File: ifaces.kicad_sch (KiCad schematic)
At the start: 33 parts, among them J3 MicroSD slot, J4 USB C, Q1 IRLML6401, Q2 BSS138, U3 USBLC6-2SC6

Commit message: more stuff
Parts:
- added J6: Display, symbol Connector:Conn_01x08_Pin
- added R16, R17, R18, R19, R20: 47k, Inductor_SMD:L_0805_2012Metric, symbol Device:R
- added R21: 1k, Inductor_SMD:L_0805_2012Metric, symbol Device:R
- added SW10, SW11, SW12, SW13, SW14, SW15, SW16, SW2, SW3, SW4, SW5, SW6, SW7, SW8, SW9: ~, symbol Switch:SW_Push_45deg
- added SW17: "OK", symbol Switch:SW_Push_45deg
- R10, R3, R4, R5, R6, R7, R8, R9: value 47R -> 27R
- R12: value 100k -> 47k
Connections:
- net +3V3: now also R21.2
- net GND: now also R16.1, R17.1, R18.1, R19.1, R20.1
- net DAT2: now reaches J3.1 (DAT2)
- net SD_DET: now reaches J3.10 (DET_A)
- net DAT3: now reaches J3.2 (DAT3/CD)
- net CMD: now reaches J3.3 (CMD)
- net CLK: now reaches J3.5 (CLK)
- net DAT0: now reaches J3.7 (DAT0)
- net DAT1: now reaches J3.8 (DAT1)
- new net: R21.1, SW17.2
- new net BOOT0: SW17.1
- new net COL_1: SW11.1, SW14.1, SW2.1, SW5.1, SW8.1
- new net COL_2: SW12.1, SW15.1, SW3.1, SW6.1, SW9.1
- new net COL_3: SW10.1, SW13.1, SW16.1, SW4.1, SW7.1
- new net ROW_1: R16.2, SW2.2, SW3.2, SW4.2
- new net ROW_2: R17.2, SW5.2, SW6.2, SW7.2
- new net ROW_3: R18.2, SW10.2, SW8.2, SW9.2
- new net ROW_4: R19.2, SW11.2, SW12.2, SW13.2
- new net ROW_5: R20.2, SW14.2, SW15.2, SW16.2
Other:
- note added: "Keyboard"
- moved on the sheet: C1, C2, C3, C4, C5, C6, D1, D2, D3, D4, D5, D6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

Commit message: imported SA868 - thanks, edgetriggered
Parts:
- renumbered C1 to C14, C2 to C15, C3 to C16, C6 to C17, C5 to C18, C4 to C19, D7 to D10, D8 to D11, D1 to D4, D2 to D5, D3 to D6, D4 to D7, D5 to D8, D6 to D9, FB1 to FB3, J3 to J4, J6 to J5, J4 to J6, Q2 to Q3, Q1 to Q4, R3 to R10, R4 to R11, R5 to R12, R6 to R13, R7 to R14, R8 to R15, R9 to R16, R10 to R17, R21 to R18, R16 to R19, R17 to R20, R18 to R21, R19 to R22, R20 to R23, R2 to R24, R1 to R25, R11 to R7, R13 to R8, R12 to R9, SW9 to SW10, SW12 to SW11, SW15 to SW12, SW4 to SW13, SW7 to SW14, SW10 to SW15, SW13 to SW16, SW16 to SW17, SW17 to SW2, SW2 to SW3, SW5 to SW4, SW8 to SW5, SW11 to SW6, SW14 to SW7, SW3 to SW8, SW6 to SW9, U3 to U5

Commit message: interfaces update
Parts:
- added C20: 10uF/10V, Capacitor_Tantalum_SMD:CP_EIA-3528-21_Kemet-B, symbol Device:C_Polarized
- added C21: 47uF/10V, Capacitor_Tantalum_SMD:CP_EIA-3528-21_Kemet-B, symbol Device:C_Polarized
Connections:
- net +3V3: now also J5.8 (Pin_8), Q4.2 (S), R9.2, C21.1
- net GND: now also J5.3 (Pin_3), C20.2, C21.2
- net ~{DISP_RST}: now reaches J5.1 (Pin_1)
- net at J5.2 (Pin_2): now also C20.1
- net ~{DISP_CE}: now reaches J5.4 (Pin_4)
- net DISP_D/C: now reaches J5.5 (Pin_5)
- net DISP_SDIN: now reaches J5.6 (Pin_6)
- net DISP_SCK: now reaches J5.7 (Pin_7)
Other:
- note added: "PCB view, left to right"
- moved on the sheet: J5

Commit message: connections
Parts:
- added D13: BAT60A, Diode_SMD:D_SOD-323, symbol Diode:BAT60A
- added J7: Vibrator, symbol Connector:Conn_01x02_Pin
- added J8: Speaker, symbol Connector:Conn_01x02_Pin
- added Q5: BSS138, Package_TO_SOT_SMD:SOT-23, symbol Transistor_FET:BSS138
- added R22: 100k, Inductor_SMD:L_0805_2012Metric, symbol Device:R
- renumbered C20 to C17, C21 to C18, C17 to C19, C18 to C20, C19 to C21, D9 to D10, D10 to D11, D11 to D12, D4 to D5, D5 to D6, D6 to D7, D7 to D8, D8 to D9, J4 to J5, J5 to J6, J6 to J9, R7 to R11, R8 to R12, R9 to R13, R10 to R14, R11 to R15, R12 to R16, R13 to R17, R14 to R18, R15 to R19, R16 to R20, R17 to R21, R18 to R23, R19 to R24, R20 to R25, R21 to R26, R22 to R27, R23 to R28, R24 to R29, R25 to R30
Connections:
- net +3V3: now also D13.1 (K), J7.1 (Pin_1)
- net GND: now also Q5.2 (S), R22.1
- new net: D13.2 (A), J7.2 (Pin_2), Q5.3 (D)
- new net SPK_N: J8.2 (Pin_2)
- new net SPK_P: J8.1 (Pin_1)
- new net VIBR: Q5.1 (G), R22.2

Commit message: audio part
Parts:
- removed J8: Speaker, symbol Connector:Conn_01x02_Pin
- renumbered J9 to J8, Q3 to Q5, Q4 to Q6, Q5 to Q7, R11 to R13, R12 to R14, R13 to R15, R14 to R16, R15 to R17, R16 to R18, R17 to R19, R18 to R20, R19 to R21, R20 to R22, R21 to R23, R22 to R24, R23 to R25, R24 to R26, R25 to R27, R26 to R28, R27 to R29, R28 to R30, R29 to R31, R30 to R32

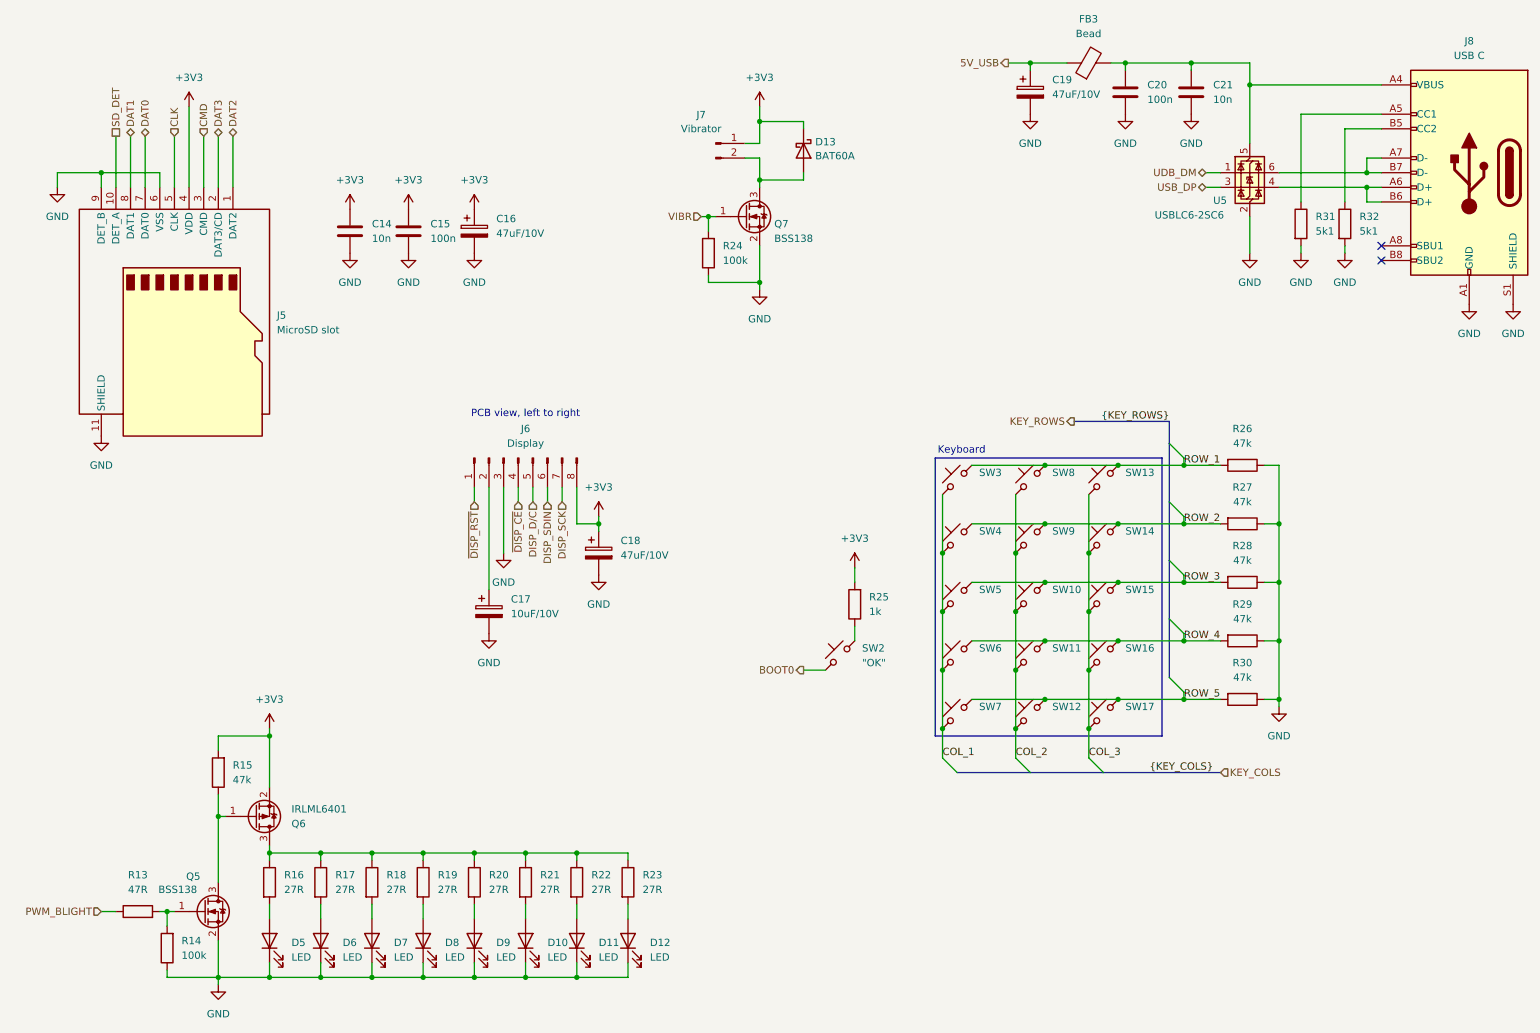
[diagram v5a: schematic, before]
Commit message: spk/mic update
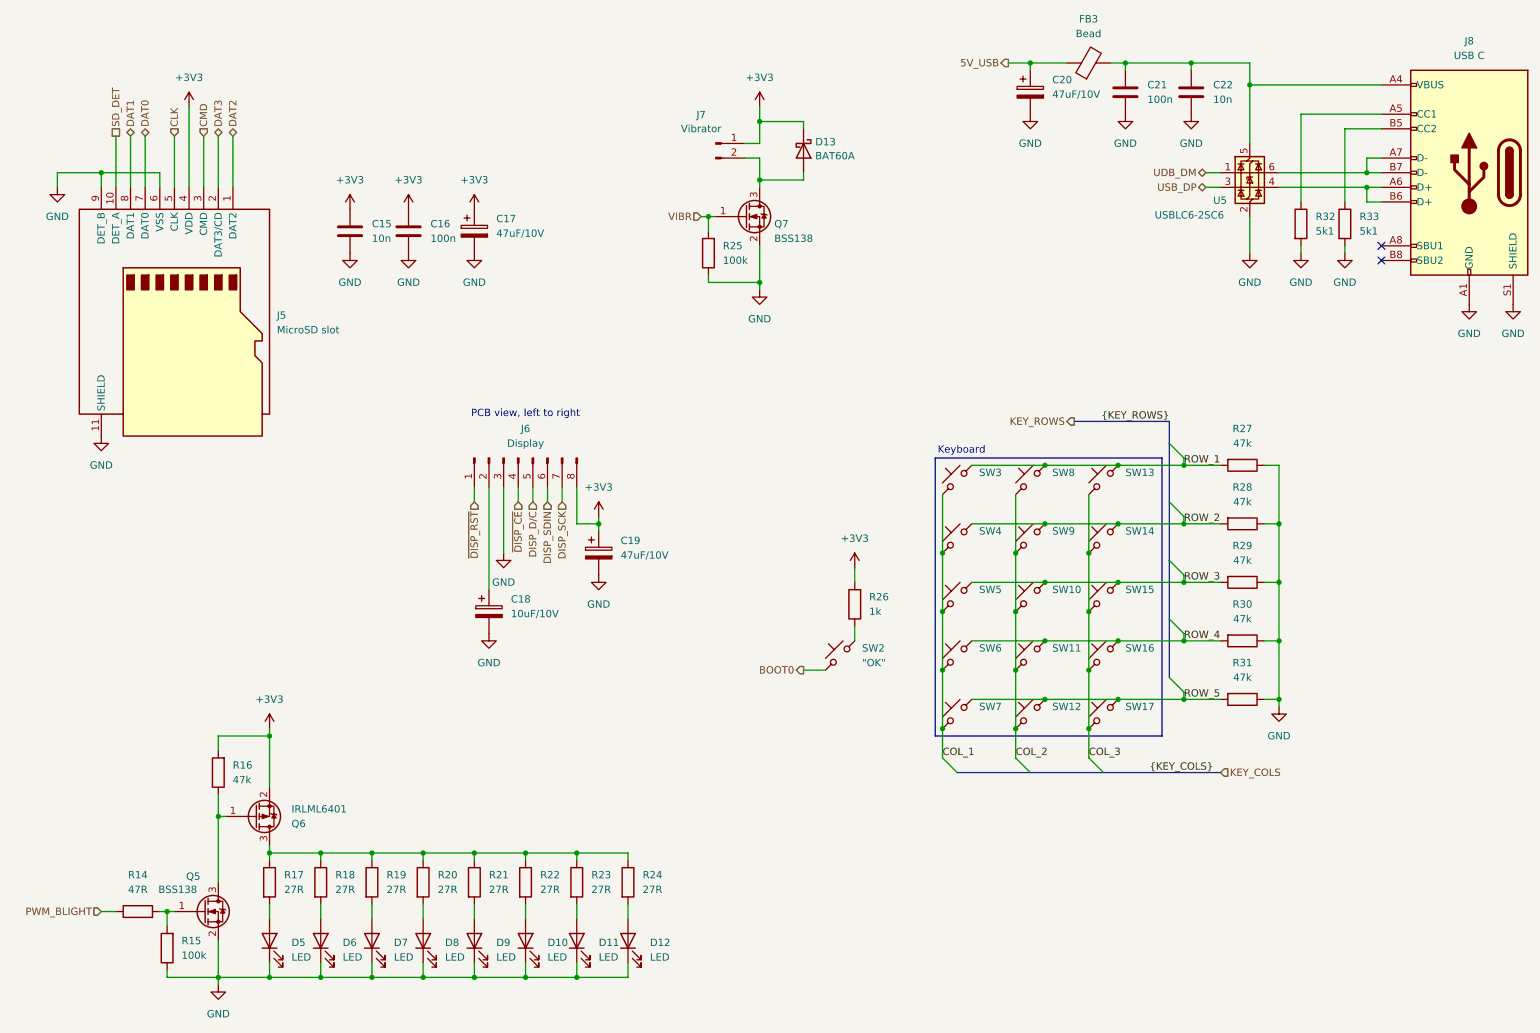
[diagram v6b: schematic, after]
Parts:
- renumbered C14 to C15, C15 to C16, C16 to C17, C17 to C18, C18 to C19, C19 to C20, C20 to C21, C21 to C22, R13 to R14, R14 to R15, R15 to R16, R16 to R17, R17 to R18, R18 to R19, R19 to R20, R20 to R21, R21 to R22, R22 to R23, R23 to R24, R24 to R25, R25 to R26, R26 to R27, R27 to R28, R28 to R29, R29 to R30, R30 to R31, R31 to R32, R32 to R33

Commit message: removed audio part
- added buzzer
- added battery voltage measurement
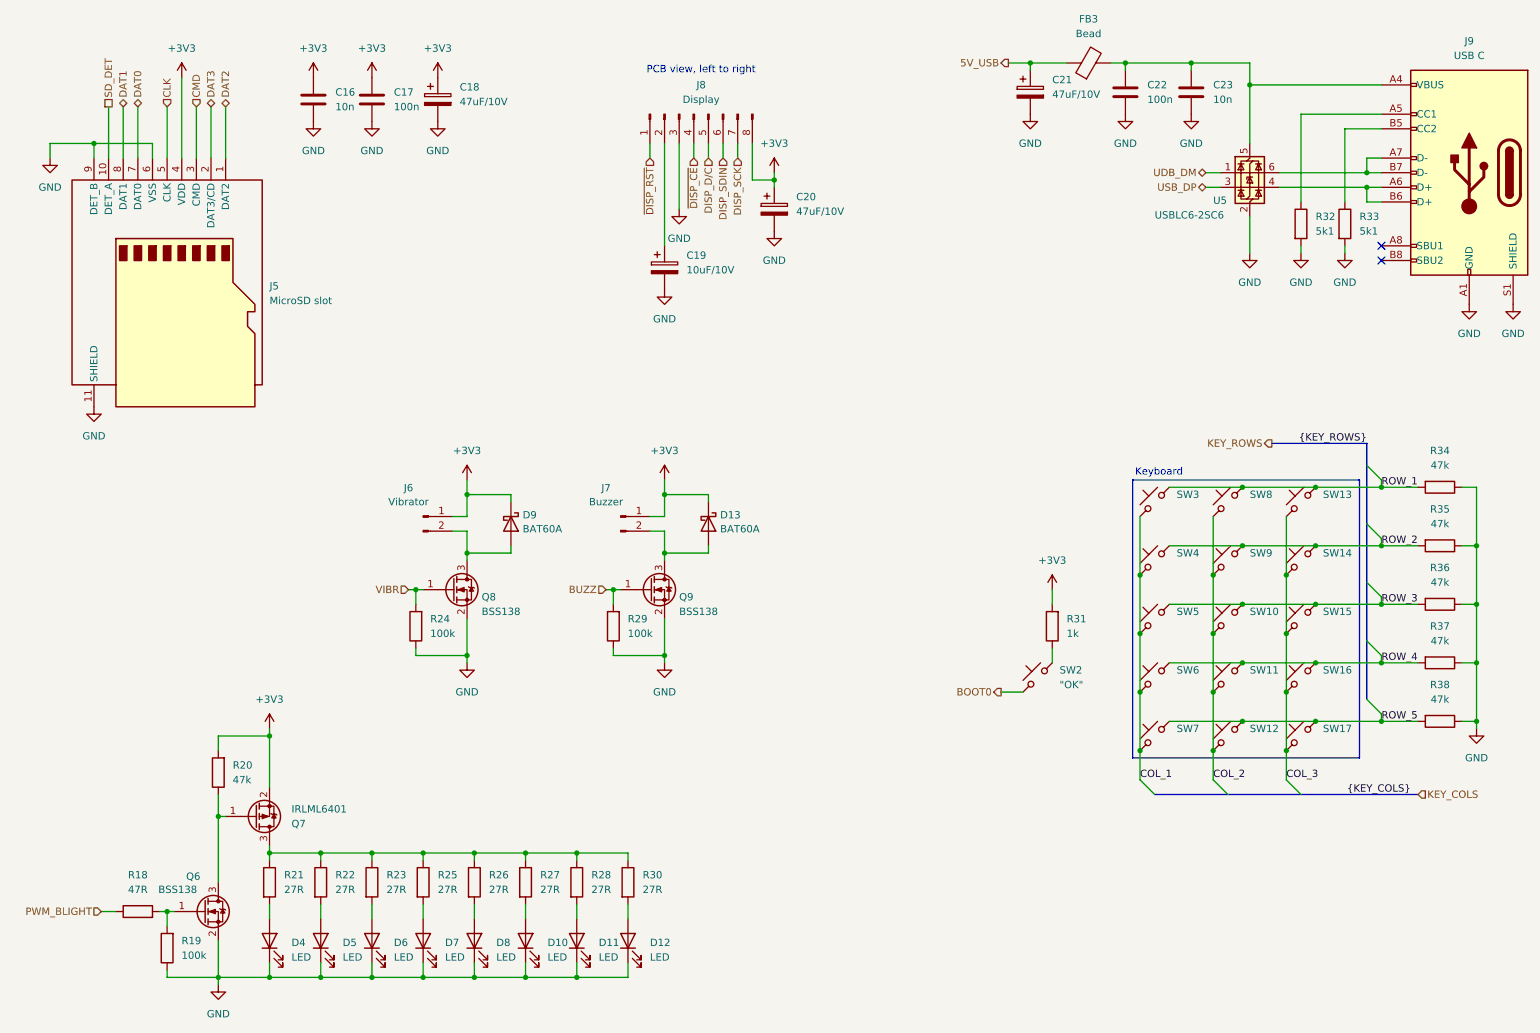
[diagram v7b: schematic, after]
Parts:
- removed C18: 10uF/10V, Capacitor_Tantalum_SMD:CP_EIA-3528-21_Kemet-B, symbol Device:C_Polarized
- removed J6: Display, symbol Connector:Conn_01x08_Pin
- added C20: 47uF/10V, Capacitor_Tantalum_SMD:CP_EIA-3528-21_Kemet-B, symbol Device:C_Polarized
- added D13: BAT60A, Diode_SMD:D_SOD-323, symbol Diode:BAT60A
- added J7: Buzzer, symbol Connector:Conn_01x02_Pin
- added J8: Display, symbol Connector:Conn_01x08_Pin
- added Q9: BSS138, Package_TO_SOT_SMD:SOT-23, symbol Transistor_FET:BSS138
- added R29: 100k, Inductor_SMD:L_0805_2012Metric, symbol Device:R
- C19: value 47uF/10V -> 10uF/10V; MPN 74-293D476X9010B2TE3 -> 581-TAJB106K010SNJ; PN 74-293D476X9010B2TE3 -> 581-TAJB106K010SNJ
- renumbered C15 to C16, C16 to C17, C17 to C18, C20 to C21, C21 to C22, C22 to C23, D5 to D4, D6 to D5, D7 to D6, D8 to D7, D9 to D8, D13 to D9, J7 to J6, J8 to J9, Q5 to Q6, Q6 to Q7, Q7 to Q8, R14 to R18, R15 to R19, R16 to R20, R17 to R21, R18 to R22, R19 to R23, R25 to R24, R20 to R25, R21 to R26, R22 to R27, R23 to R28, R24 to R30, R26 to R31, R27 to R34, R28 to R35, R29 to R36, R30 to R37, R31 to R38
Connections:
- net +3V3: now also C20.1, D13.1 (K), J7.1 (Pin_1), J8.8 (Pin_8); no longer C19.1
- net DISP_D/C: now also J8.5 (Pin_5)
- net DISP_SCK: now also J8.7 (Pin_7)
- net DISP_SDIN: now also J8.6 (Pin_6)
- net GND: now also C20.2, J8.3 (Pin_3), Q9.2 (S), R29.1
- net ~{DISP_CE}: now also J8.4 (Pin_4)
- net ~{DISP_RST}: now also J8.1 (Pin_1)
- new net: D13.2 (A), J7.2 (Pin_2), Q9.3 (D)
- new net: C19.1, J8.2 (Pin_2)
- new net BUZZ: Q9.1 (G), R29.2
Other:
- moved on the sheet: C16, C17, C18, D9, J5, J6, Q8, R24, R31, R34, R35, R36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

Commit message: mayhem
- removed sd card slot
- started pcb design
- added nice 3310 photos
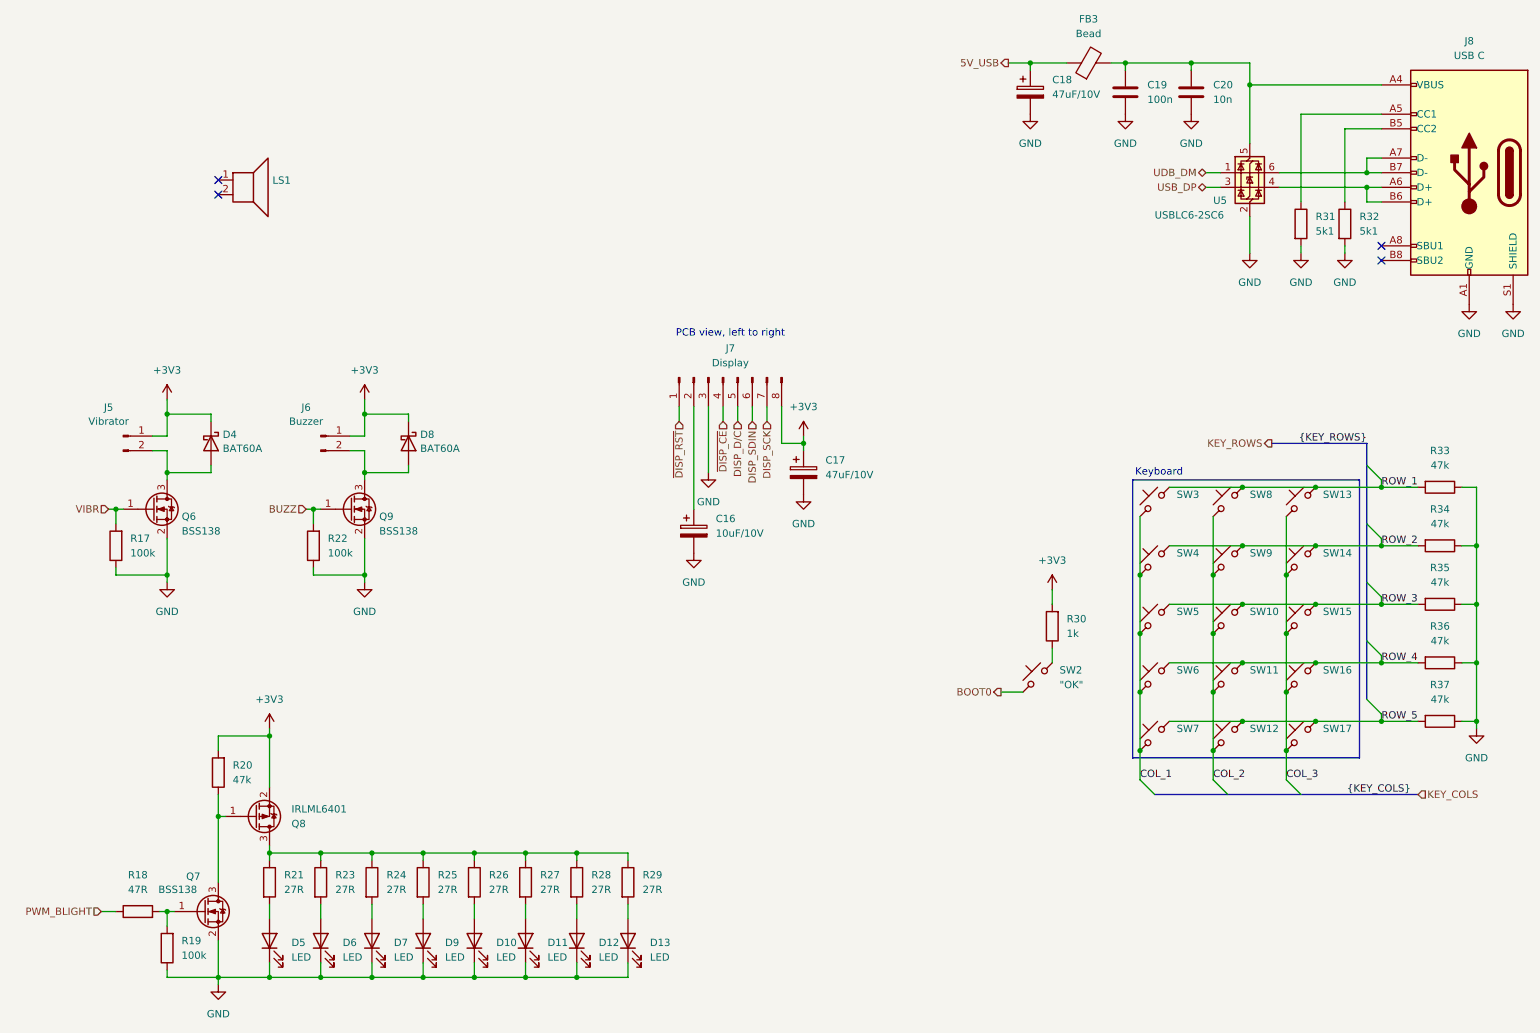
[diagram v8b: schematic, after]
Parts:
- removed C16: 10n, Capacitor_SMD:C_0805_2012Metric, symbol Device:C
- removed C17: 100n, Capacitor_SMD:C_0805_2012Metric, symbol Device:C
- removed C18: 47uF/10V, Capacitor_Tantalum_SMD:CP_EIA-3528-21_Kemet-B, symbol Device:C_Polarized
- removed J5: MicroSD slot, Connector_Card:microSD_HC_Hirose_DM3AT-SF-PEJM5, symbol Connector:Micro_SD_Card_Det_Hirose_DM3AT
- added LS1: ~, Parts:3310_speaker, symbol Device:Speaker
- J7: renamed from J8; footprint (none) -> Parts:3310_display
- J8: renamed from J9; footprint Connector_USB:USB_C_Receptacle_JAE_DX07S016JA1R1500 -> Connector_USB:USB_C_Receptacle_GCT_USB4110
- SW10, SW11, SW12, SW13, SW14, SW15, SW16, SW17, SW2, SW3, SW4, SW5, SW6, SW7, SW8, SW9: footprint (none) -> Parts:3310_key
- renumbered C19 to C16, C20 to C17, C21 to C18, C22 to C19, C23 to C20, D8 to D10, D10 to D11, D11 to D12, D12 to D13, D9 to D4, D4 to D5, D5 to D6, D6 to D7, D13 to D8, D7 to D9, J6 to J5, J7 to J6, Q8 to Q6, Q6 to Q7, Q7 to Q8, R24 to R17, R29 to R22, R22 to R23, R23 to R24, R30 to R29, R31 to R30, R32 to R31, R33 to R32, R34 to R33, R35 to R34, R36 to R35, R37 to R36, R38 to R37
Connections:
- no-connect marks 2 -> 4
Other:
- moved on the sheet: C16, C17, D4, D8, J5, J6, J7, Q6, Q9, R17, R22
